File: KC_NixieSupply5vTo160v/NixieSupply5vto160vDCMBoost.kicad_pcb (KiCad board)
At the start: 2 copper layers, 38.2 x 37.9 mm, 47 parts, among them J1 Screw_Terminal_1x04, J2 CONN_01X01, J3 CONN_01X01, J4 CONN_01X01, J5 CONN_01X01, P1 USB_OTG, Q1 FDS2734CT, Q26 MMBTA42, U1 UCC3803

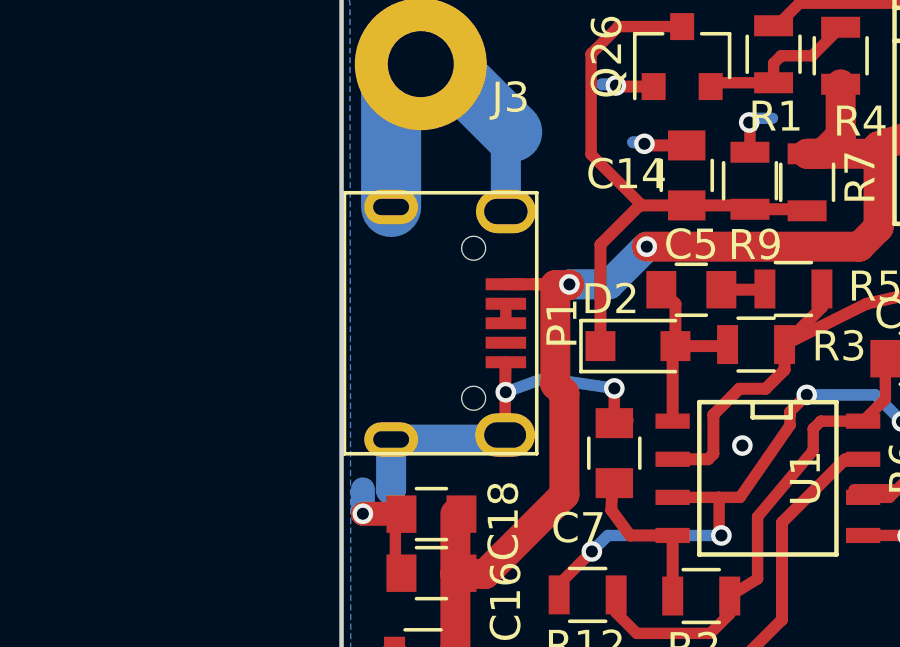
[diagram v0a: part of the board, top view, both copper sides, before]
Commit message: New Gerber Files
Updated the layout of the USB connector to remove the Slots and replace
with holes.
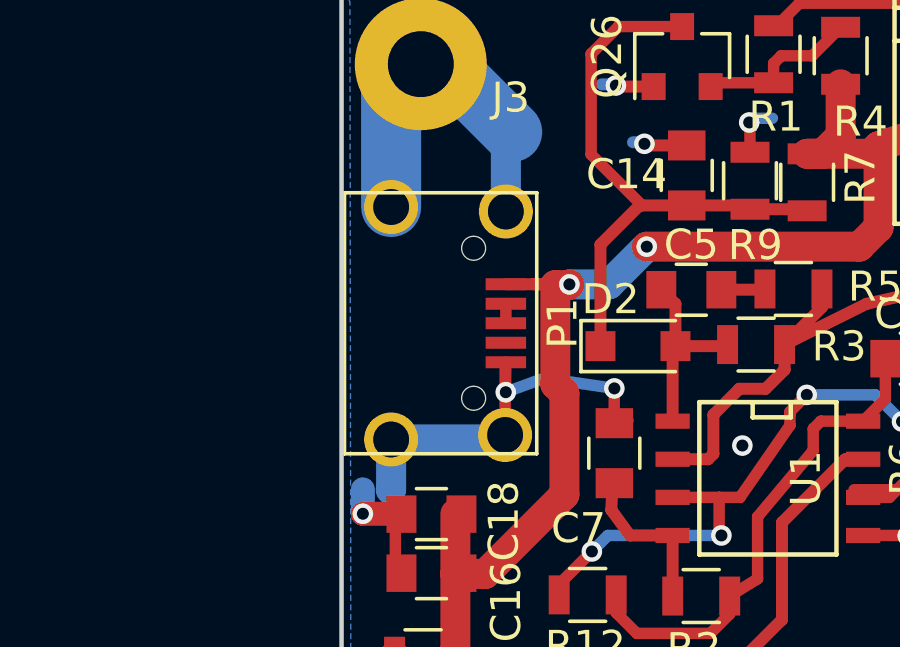
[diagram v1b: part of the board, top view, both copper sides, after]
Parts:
- C15: value 330pF 250v -> 47pF 250v
- L3: value 47uH -> 33uH
- P1: footprint NixieSupply5vto160vDCMBoost_socket:USB_Micro-B_Wurth_3A -> NixieSupply5vto160vDCMBoost_socket:USB_Micro-B_Wurth_3A_Non-OVAL-Drill
- Q1: value FDS2734CT -> FDS2672CT
- R16: value 8.06k -> 7.68k
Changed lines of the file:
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@@
     (links 87)
     (no_connects 0)
-    (area 17.081499 66.616595 229.894856 177.128)
+    (area 135.992799 73.127799 174.369801 111.187301)
     (thickness 1.6)
     (drawings 10)
@@
       (effects (font (size 1 1) (thickness 0.15)))
     )
-    (fp_text value 8.06k (at 0 1.75 90) (layer F.Fab)
+    (fp_text value 7.68k (at 0 1.75 90) (layer F.Fab)
       (effects (font (size 1 1) (thickness 0.15)))
     )
@@
       (effects (font (size 1 1) (thickness 0.15)))
     )
-    (fp_text value "330pF 250v" (at 0 1.5) (layer F.Fab)
+    (fp_text value "47pF 250v" (at 0 1.5) (layer F.Fab)
       (effects (font (size 1 1) (thickness 0.15)))
     )
@@
       (effects (font (size 1 1) (thickness 0.15)))
     )
-    (fp_text value FDS2734CT (at 0 1.27 180) (layer F.Fab)
+    (fp_text value FDS2672CT (at 0 1.27 180) (layer F.Fab)
       (effects (font (size 1 1) (thickness 0.15)))
     )
@@
       (effects (font (size 1 1) (thickness 0.15)))
     )
-    (fp_text value 47uH (at 0 8.89 180) (layer F.Fab)
+    (fp_text value 33uH (at 0 8.89 180) (layer F.Fab)
       (effects (font (size 1 1) (thickness 0.15)))
     )
@@
     )
   )
-  (module NixieSupply5vto160vDCMBoost_socket:USB_Micro-B_Wurth_3A (layer F.Cu)
+  (module NixieSupply5vto160vDCMBoost_socket:SOIC-8-N (layer F.Cu)
+    (at 150.2791 89.6747 270)
+    (descr "Module Narrow CMS SOJ 8 pins large")
+    (tags "CMS SOJ")
+    (attr smd)
+    (fp_text reference U1 (at 0 -1.27 270) (layer F.SilkS)
+      (effects (font (size 1 1) (thickness 0.15)))
+    )
+    (fp_text value UCC3803 (at 0 1.27 270) (layer F.Fab)
+      (effects (font (size 1 1) (thickness 0.15)))
+    )
+    (fp_text user %R (at 0 -1.3 270) (layer F.Fab)
+      (effects (font (size 1 1) (thickness 0.15)))
+    )
+    (fp_line (start -2.54 -2.286) (end 2.54 -2.286) (layer F.SilkS) (width 0.15))
+    (fp_line (start 2.54 -2.286) (end 2.54 2.286) (layer F.SilkS) (width 0.15))
+    (fp_line (start 2.54 2.286) (end -2.54 2.286) (layer F.SilkS) (width 0.15))
+    (fp_line (start -2.54 2.286) (end -2.54 -2.286) (layer F.SilkS) (width 0.15))
+    (fp_line (start -2.54 -0.762) (end -2.032 -0.762) (layer F.SilkS) (width 0.15))
+    (fp_line (start -2.032 -0.762) (end -2.032 0.508) (layer F.SilkS) (width 0.15))
+    (fp_line (start -2.032 0.508) (end -2.54 0.508) (layer F.SilkS) (width 0.15))
+    (pad 8 smd rect (at -1.905 -3.175 270) (size 0.508 1.143) (layers F.Cu F.Paste F.Mask)
+      (net 23 "Net-(C10-Pad1)"))
+    (pad 7 smd rect (at -0.635 -3.175 270) (size 0.508 1.143) (layers F.Cu F.Paste F.Mask)
+      (net 20 "Net-(C4-Pad1)"))
+    (pad 6 smd rect (at 0.635 -3.175 270) (size 0.508 1.143) (layers F.Cu F.Paste F.Mask)
+      (net 9 "Net-(R6-Pad2)"))
+    (pad 5 smd rect (at 1.905 -3.175 270) (size 0.508 1.143) (layers F.Cu F.Paste F.Mask)
+      (net 1 GND))
+    (pad 4 smd rect (at 1.905 3.175 270) (size 0.508 1.143) (layers F.Cu F.Paste F.Mask)
+      (net 4 "Net-(C7-Pad1)"))
+    (pad 3 smd rect (at 0.635 3.175 270) (size 0.508 1.143) (layers F.Cu F.Paste F.Mask)
+      (net 5 "Net-(C11-Pad1)"))
+    (pad 2 smd rect (at -0.635 3.175 270) (size 0.508 1.143) (layers F.Cu F.Paste F.Mask)
+      (net 17 "Net-(C6-Pad2)"))
+    (pad 1 smd rect (at -1.905 3.175 270) (size 0.508 1.143) (layers F.Cu F.Paste F.Mask)
+      (net 2 "Net-(C5-Pad1)"))
+    (model SMD_Packages.3dshapes/SOIC-8-N.wrl
+      (at (xyz 0 0 0))
+      (scale (xyz 0.5 0.38 0.5))
+      (rotate (xyz 0 0 0))
+    )
+  )
+  (module NixieSupply5vto160vDCMBoost_socket:USB_Micro-B_Wurth_3A_Non-OVAL-Drill (layer F.Cu)
     (at 140.1953 84.5058 270)
     (descr "Micro USB Type B Receptacle")
@@
     (pad 5 smd rect (at 1.3 -1.35) (size 1.35 0.4) (layers F.Cu F.Paste F.Mask)
       (net 1 GND))
-    (pad 6 thru_hole oval (at -3.725 -1.35) (size 2 1.45) (drill oval 1.45 0.85) (layers *.Cu *.Mask)
-      (net 1 GND))
-    (pad 6 thru_hole oval (at 3.725 -1.325) (size 2 1.45) (drill oval 1.4 0.85) (layers *.Cu *.Mask)
-      (net 1 GND))
-    (pad 6 thru_hole oval (at -3.875 2.475) (size 1.8 1.15) (drill oval 1.2 0.55) (layers *.Cu *.Mask)
-      (net 1 GND))
-    (pad 6 thru_hole oval (at 3.875 2.475) (size 1.8 1.15) (drill oval 1.2 0.55) (layers *.Cu *.Mask)
+    (pad 6 thru_hole circle (at -3.725 -1.35) (size 1.8 1.8) (drill 1.2) (layers *.Cu *.Mask)
+      (net 1 GND))
+    (pad 6 thru_hole circle (at 3.725 -1.325) (size 1.8 1.8) (drill 1.2) (layers *.Cu *.Mask)
+      (net 1 GND))
+    (pad 6 thru_hole circle (at -3.875 2.475) (size 1.8 1.8) (drill 1.2) (layers *.Cu *.Mask)
+      (net 1 GND))
+    (pad 6 thru_hole circle (at 3.875 2.475) (size 1.8 1.8) (drill 1.2) (layers *.Cu *.Mask)
       (net 1 GND))
     (pad "" np_thru_hole circle (at 2.5 -0.275 270) (size 0.8 0.8) (drill 0.8) (layers *.Cu))
@@
       (rotate (xyz 0 0 0))
     )
-  )
-  (module NixieSupply5vto160vDCMBoost_socket:SOIC-8-N (layer F.Cu)
-    (at 150.2791 89.6747 270)
-    (descr "Module Narrow CMS SOJ 8 pins large")
-    (tags "CMS SOJ")
-    (attr smd)
-    (fp_text reference U1 (at 0 -1.27 270) (layer F.SilkS)
-      (effects (font (size 1 1) (thickness 0.15)))
-    )
-    (fp_text value UCC3803 (at 0 1.27 270) (layer F.Fab)
-      (effects (font (size 1 1) (thickness 0.15)))
-    )
-    (fp_text user %R (at 0 -1.3 270) (layer F.Fab)
-      (effects (font (size 1 1) (thickness 0.15)))
-    )
-    (fp_line (start -2.54 -2.286) (end 2.54 -2.286) (layer F.SilkS) (width 0.15))
-    (fp_line (start 2.54 -2.286) (end 2.54 2.286) (layer F.SilkS) (width 0.15))
-    (fp_line (start 2.54 2.286) (end -2.54 2.286) (layer F.SilkS) (width 0.15))
-    (fp_line (start -2.54 2.286) (end -2.54 -2.286) (layer F.SilkS) (width 0.15))
-    (fp_line (start -2.54 -0.762) (end -2.032 -0.762) (layer F.SilkS) (width 0.15))
-    (fp_line (start -2.032 -0.762) (end -2.032 0.508) (layer F.SilkS) (width 0.15))
-    (fp_line (start -2.032 0.508) (end -2.54 0.508) (layer F.SilkS) (width 0.15))
-    (pad 8 smd rect (at -1.905 -3.175 270) (size 0.508 1.143) (layers F.Cu F.Paste F.Mask)
-      (net 23 "Net-(C10-Pad1)"))
-    (pad 7 smd rect (at -0.635 -3.175 270) (size 0.508 1.143) (layers F.Cu F.Paste F.Mask)
-      (net 20 "Net-(C4-Pad1)"))
-    (pad 6 smd rect (at 0.635 -3.175 270) (size 0.508 1.143) (layers F.Cu F.Paste F.Mask)
-      (net 9 "Net-(R6-Pad2)"))
-    (pad 5 smd rect (at 1.905 -3.175 270) (size 0.508 1.143) (layers F.Cu F.Paste F.Mask)
-      (net 1 GND))
-    (pad 4 smd rect (at 1.905 3.175 270) (size 0.508 1.143) (layers F.Cu F.Paste F.Mask)
-      (net 4 "Net-(C7-Pad1)"))
-    (pad 3 smd rect (at 0.635 3.175 270) (size 0.508 1.143) (layers F.Cu F.Paste F.Mask)
-      (net 5 "Net-(C11-Pad1)"))
-    (pad 2 smd rect (at -0.635 3.175 270) (size 0.508 1.143) (layers F.Cu F.Paste F.Mask)
-      (net 17 "Net-(C6-Pad2)"))
-    (pad 1 smd rect (at -1.905 3.175 270) (size 0.508 1.143) (layers F.Cu F.Paste F.Mask)
-      (net 2 "Net-(C5-Pad1)"))
-    (model SMD_Packages.3dshapes/SOIC-8-N.wrl
-      (at (xyz 0 0 0))
-      (scale (xyz 0.5 0.38 0.5))
-      (rotate (xyz 0 0 0))
-    )
